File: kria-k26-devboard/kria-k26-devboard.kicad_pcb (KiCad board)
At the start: 8 copper layers, 118 x 100 mm, 476 parts, among them IC1 USB5534B-5000JZX, IC2 TPS2378DDA, J1 47272-0001, J10 USB4105-GF-A, J11 DC_SOCKET, J2 1140084168, J3 WE_68715014522, J4 SSW-106-02-G-D-RA, J5 5-2337992-8, J6 22-23-2021, J7 BM08B-SRSS-TB-LF-SN, J8 1050170001, J9 0878311420, M1 XILINX-KRIA-K26, P1 2199119-6, Q1 BSS123, Q10 BSS138-7-F, Q11 BSS138-7-F, Q12 DTC014TEBTL, Q13 DTC014TEBTL, Q14 DTC014TEBTL, Q15 PJA3441, Q16 BSS138-7-F, Q2 AO3401A, Q3 BSS138-7-F, Q4 BSS138DW-7-F, Q5 PJA3441, Q6 BSS138-7-F, Q7 BSS138-7-F, Q8 BSS138-7-F, Q9 BSS138-7-F, U1 SN74AVC4T245PWR, U10 PCA9306D_118, U11 M24C64-FMC6TG, U12 TPD4E05U06QDQARQ1, U13 TPD4E05U06QDQARQ1, U14 USB3310C-CP, U15 TPD4E05U06QDQARQ1, U16 TPD4E05U06QDQARQ1, U17 GSB3112311HR, U18 TPD4E05U06QDQARQ1, U19 TPD4E05U06QDQARQ1, U2 FIN1019MTC, U20 GSB3112311HR, U21 DP83867CRRGZR, U22 TPS3840PH30DBVR, U23 TPS3840PH30DBVR, U24 SN74AVC4T245PWR, U25 SN74AVC2T245RSWR, U26 SN74LVC1G125DBVR, U27 74LV07ATPWJ, U28 MCP1799-3302H_DB, U29 MCP1799-3302H_DB, U3 TPD4E05U06QDQARQ1, U30 FT4232HPQ, U31 93LC56CT-IMC, U32 SN74AVC4T245PWR, U33 SN74AVC4T245PWR, U34 SN74AVC2T245RSWR, U35 SN74AVC2T245RSWR, U36 NC7WZ07P6X, U37 RPX-4.0-R, U38 AP62301WU-7, U39 AP62301WU-7, U4 NVT4858HKZ, U40 AP62301WU-7, U41 AP62301WU-7, U42 AP62301WU-7, U43 AP62301WU-7, U44 AP62301WU-7, U45 AP62301WU-7, U46 LTC4358CDE, U47 LTC4358CDE, U48 LTC4358CDE, U5 TPS2116DRLR, U6 SI53152-A01AGMR, U7 SN65LVDS1DR, U8 XLL736027.000000X, U9 PI4MSD5V9540BUEX, Y1 SIT9120AI-2C3-33E100.000000X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

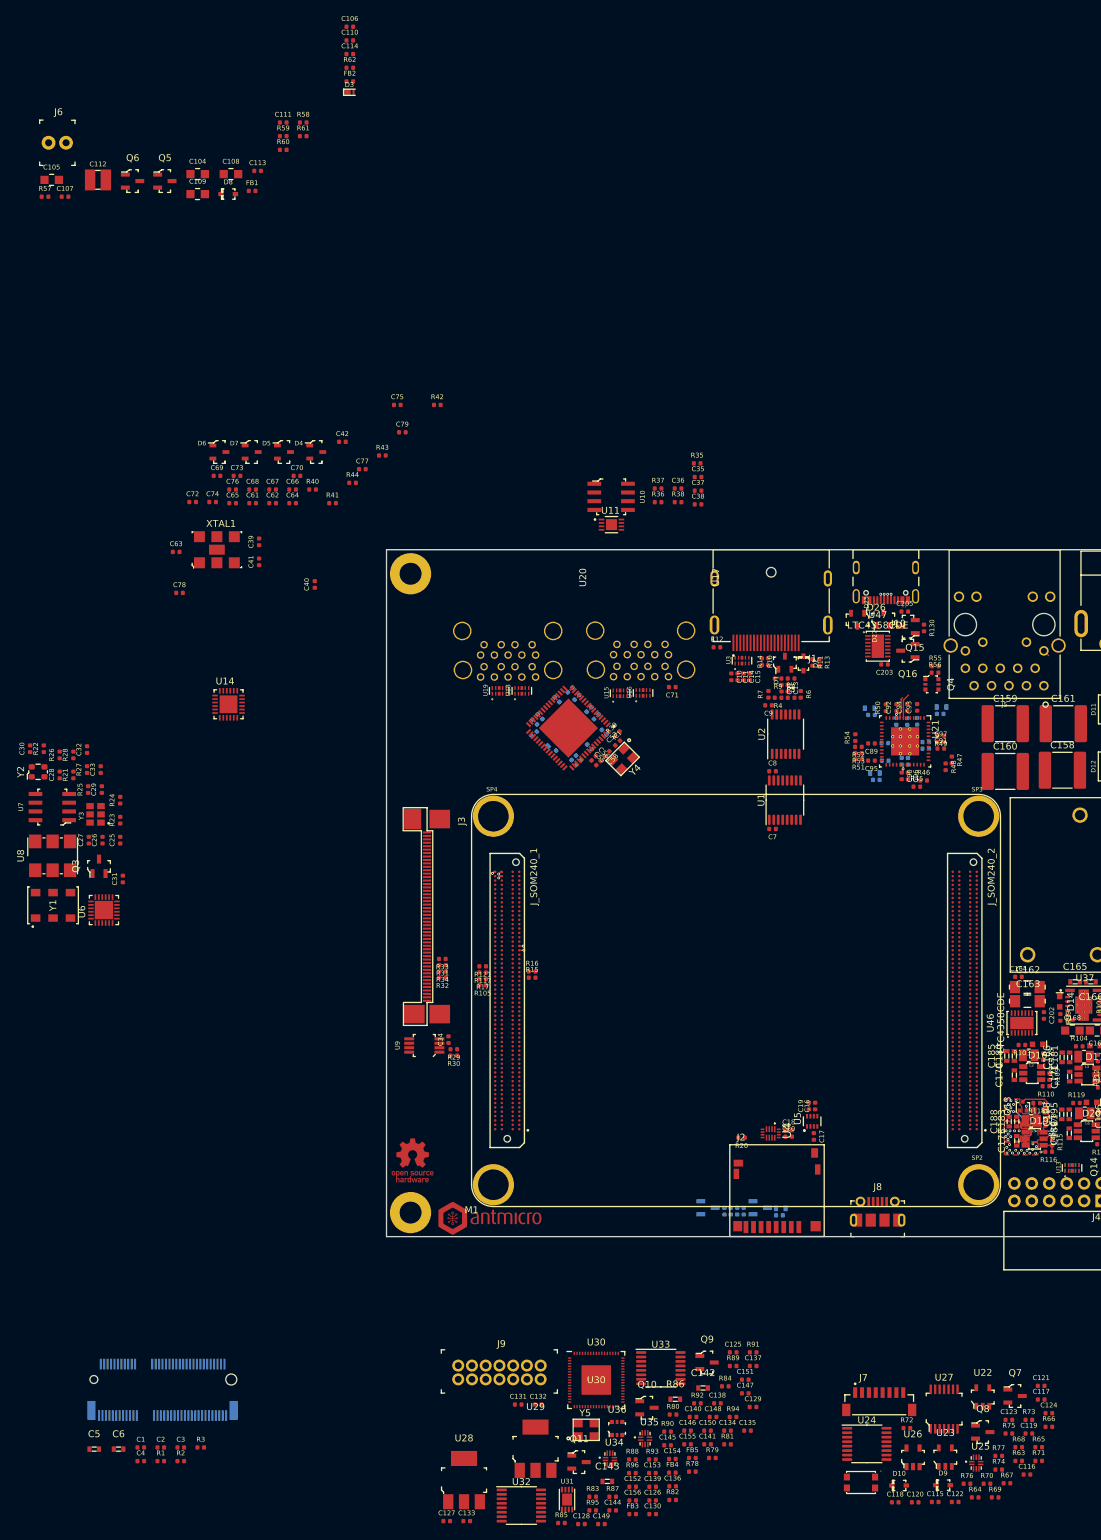
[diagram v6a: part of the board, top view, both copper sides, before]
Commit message: Finished initial component placement
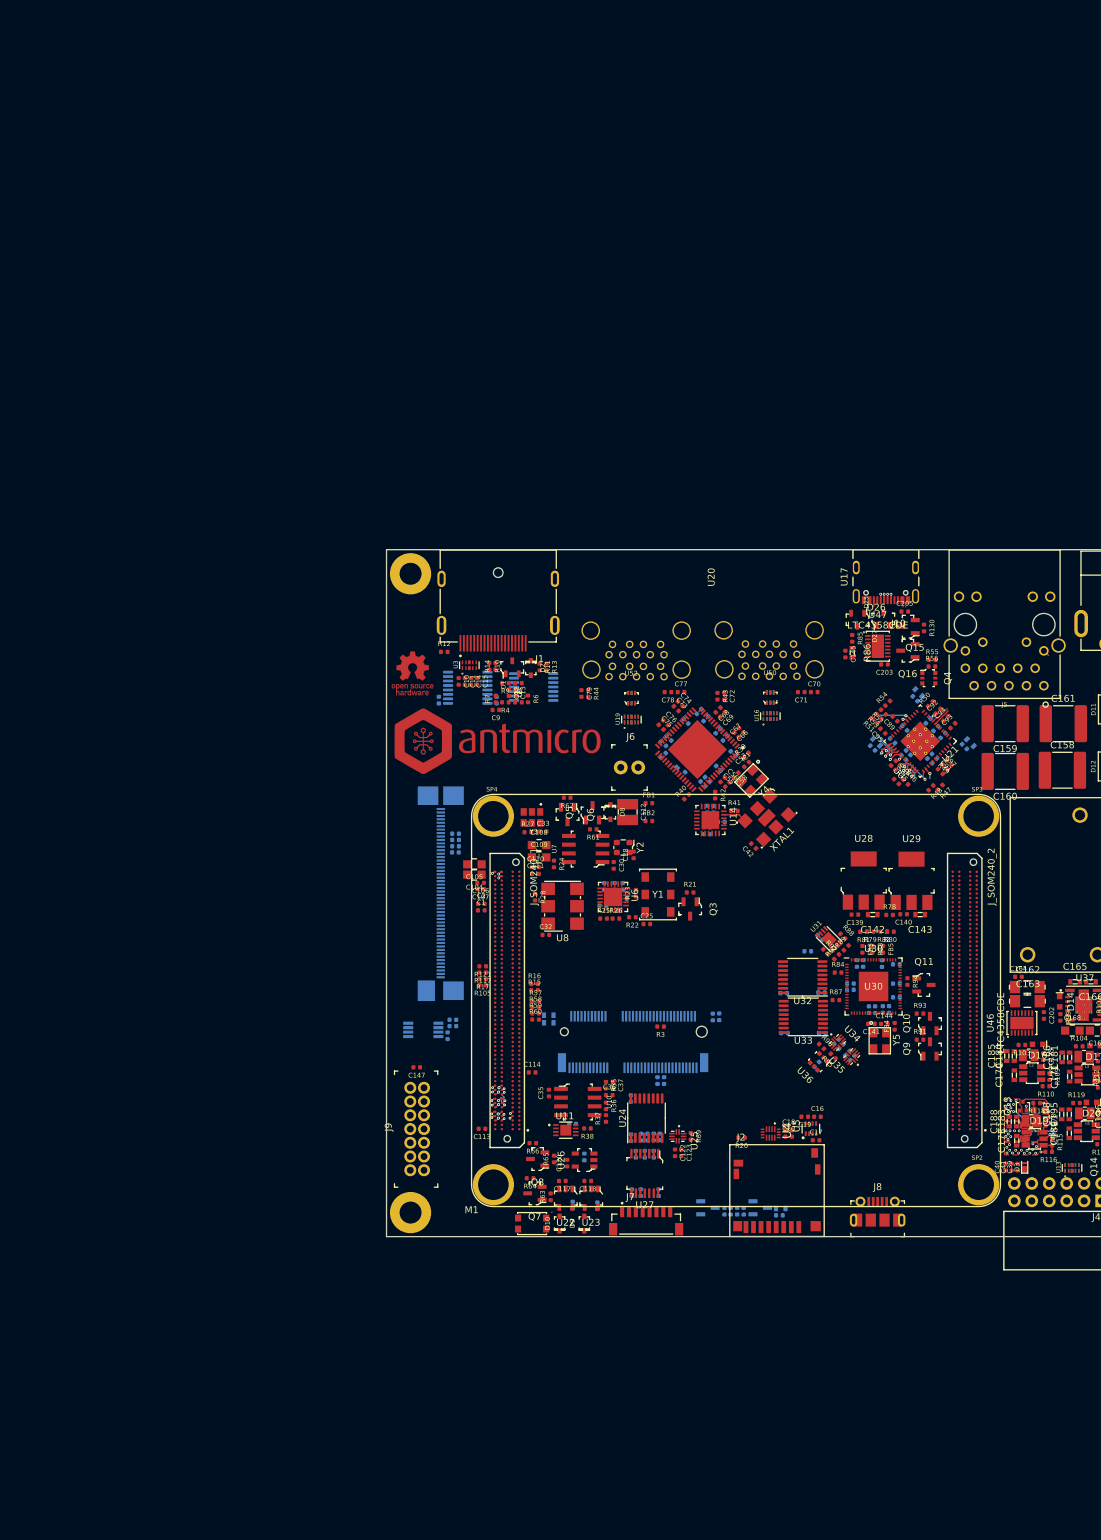
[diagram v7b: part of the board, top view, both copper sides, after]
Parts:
- removed D4, D5, D6, D7: PESD2USB5UV-TR, antmicro-footprints:SOT-23s
- added C207: C_100n_0402, antmicro-footprints:0402-cap, B.Cu at (107.7, 104.1)
- added U49: WE-TVS-82400152, antmicro-footprints:SOT-563, B.Cu at (129.9, 73.5)
- added U50: WE-TVS-82400152, antmicro-footprints:SOT-563, F.Cu at (129.9, 73.5)
- added U51: WE-TVS-82400152, antmicro-footprints:SOT-563, B.Cu at (109.7, 73.6)
- added U52: WE-TVS-82400152, antmicro-footprints:SOT-563, F.Cu at (109.7, 73.6)
- C115, C116, C119, C121, C124, C125, C126, C127, C128, C129, C130, C131, C132, C133, C134, C135, C136, C137, C138, C146, C148, C149, C150, C151, C152, C153, C154, C155, C156, C26, C27, C29, C3, C31, C34, C38, C4, C5, C6, C61, C62, C63, C64, C65, C7, C8, J3, R1, R2, R29, R30, R31, R32, R33, R34, R67, R68, R70, R71, R72, R73, R74, R75, R76, R77, U1, U15, U18, U2, U9: moved to B.Cu
- N2: footprint antmicro-footprints:antmicro-logo_scaled_15mm -> antmicro-footprints:antmicro-logo_scaled_30mm
- moved D3 184.8 mm to (166.9, 141.9), turned to 90 degrees
- moved C114 150.6 mm to (95.2, 128.1)
- moved C113 143.2 mm to (87.9, 136.3), turned to 180 degrees
- moved C39 143.1 mm to (165.9, 141.9)
- moved C41 140.6 mm to (165.0, 141.9)
- moved R57 137.2 mm to (95.7, 117.7)
- moved R85 135.6 mm to (141.8, 64.9), turned to 270 degrees
- moved R58 133.2 mm to (95.7, 118.6)
- moved R59 132.9 mm to (95.7, 119.5)
- moved R60 131.8 mm to (95.7, 120.4)
- moved C40 131.6 mm to (164.1, 141.9)
- moved C106 126.1 mm to (87.7, 100.5), turned to 180 degrees
- moved C110 123.3 mm to (95.7, 98.2)
- moved J6 123.3 mm to (108.1, 83.7)
- moved C112 120.1 mm to (109.1, 90.2), turned to 270 degrees
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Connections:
- C132 pad 1: GND -> PS_3V3
- C132 pad 2: /Debug and JTAG/USB_3V3 -> GND
- U17 pad 11: /USB/USB2_N -> Net-(U17-Pad11)
- U17 pad 12: /USB/USB2_P -> Net-(U17-Pad12)
- U17 pad 2: /USB/USB1_N -> Net-(U17-Pad2)
- U17 pad 3: /USB/USB1_P -> Net-(U17-Pad3)
- U20 pad 11: /USB/USB4_N -> Net-(U20-Pad11)
- U20 pad 12: /USB/USB4_P -> Net-(U20-Pad12)
- U20 pad 2: /USB/USB3_N -> Net-(U20-Pad2)
- U20 pad 3: /USB/USB3_P -> Net-(U20-Pad3)
- U27 pad 1: Net-(R68-Pad2) -> Net-(R69-Pad2)
- U27 pad 10: /PCIE M2 key E /~M2_PERST -> /Reset logic/~SD_CARD_RESET
- U27 pad 11: Net-(R69-Pad2) -> Net-(R68-Pad2)
- U27 pad 2: /Reset logic/~SD_CARD_RESET -> /PCIE M2 key E /~M2_PERST
- U27 pad 3: Net-(R70-Pad2) -> Net-(R72-Pad2)
- U27 pad 4: /Reset logic/~USB_PHY_RESET -> /Ethernet/~ETH_RESET
- U27 pad 8: /Ethernet/~ETH_RESET -> /Reset logic/~USB_PHY_RESET
- U27 pad 9: Net-(R72-Pad2) -> Net-(R70-Pad2)
- U30 pad 51: /Debug and JTAG/USB_3V3 -> Net-(U30-Pad51)
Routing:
- net /Ethernet/MIO69: track 0.00 -> 5.41 mm, vias 0 -> 1
- net /Ethernet/MIO65: track 0.00 -> 5.33 mm, vias 0 -> 1
- net /Camera interface/HPA04_P: track 0.00 -> 5.13 mm, vias 0 -> 1
- net /Ethernet/MIO66: track 0.00 -> 4.98 mm, vias 0 -> 1
- net /Ethernet/MIO76: track 0.00 -> 4.59 mm, vias 0 -> 1
- net /Camera interface/HPA04_N: track 0.00 -> 4.48 mm, vias 0 -> 1
- net /Camera interface/HPA02_P: track 0.00 -> 3.65 mm, vias 0 -> 1
- net /Camera interface/HPA02_N: track 0.00 -> 3.54 mm, vias 0 -> 1
- net GND: track 4.83 -> 8.36 mm, vias 16 -> 22
- net /Camera interface/HPA01_P: track 0.00 -> 3.51 mm, vias 0 -> 1
- net Net-(U14-Pad23): track 0.00 -> 3.46 mm
- net /Camera interface/HPA01_N: track 0.00 -> 3.33 mm, vias 0 -> 1
- net /Camera interface/HPA03_P: track 0.00 -> 2.53 mm, vias 0 -> 1
- net /Ethernet/MIO72: track 0.00 -> 2.30 mm, vias 0 -> 1
- net /Ethernet/MIO68: track 0.00 -> 2.23 mm, vias 0 -> 1
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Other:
- net class Default: via_dia 0.55 -> 0.45; via_drill 0.3 -> 0.2
- net class ipedance_internal added: clearance 0.125, trace_width 0.155, via_dia 0.4, via_drill 0.15

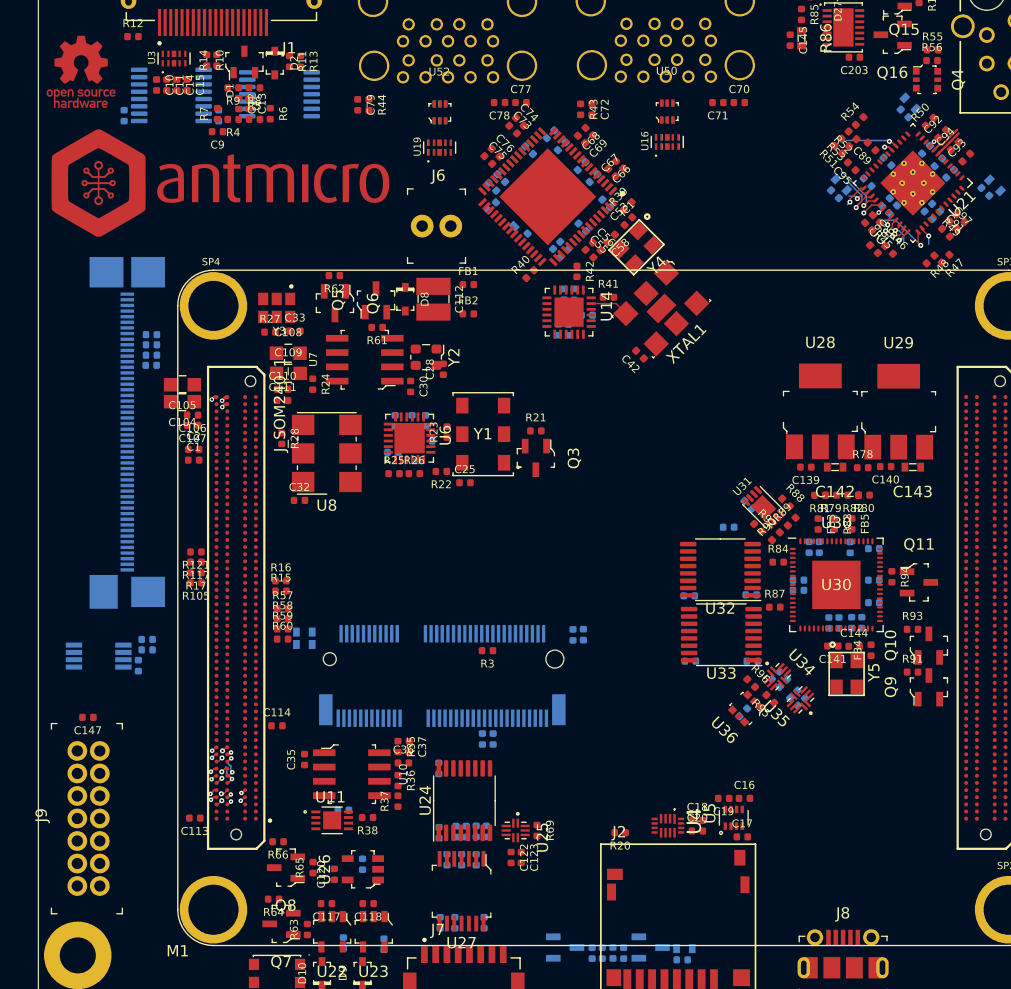
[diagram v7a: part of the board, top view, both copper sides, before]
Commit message: Component size optimization, SOM connector fanout, routing of camera interface
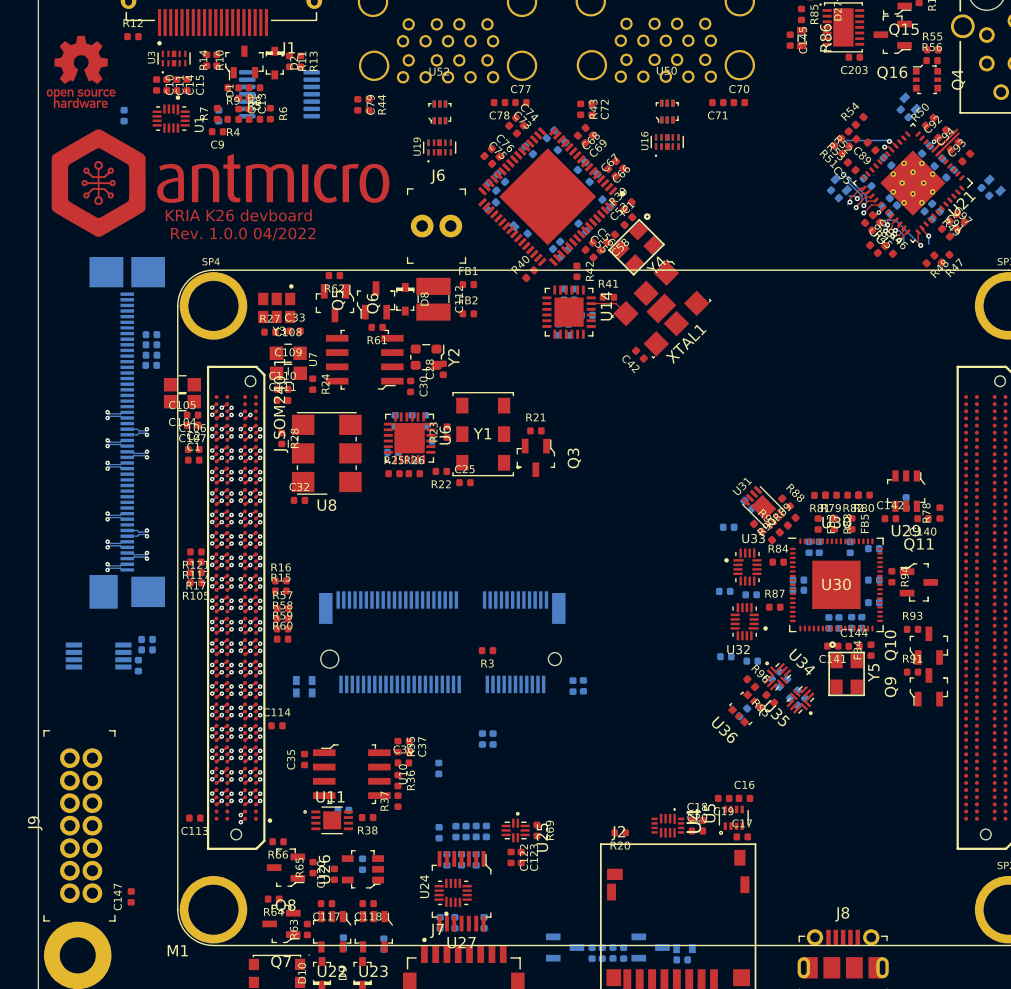
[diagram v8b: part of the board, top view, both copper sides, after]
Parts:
- removed C143: C_10u_0603, antmicro-footprints:0603-cap
- removed U28: MCP1799-3302H_DB, antmicro-footprints:SOT-223
- C139: moved to B.Cu
- C142: value C_10u_0603 -> C_100n_0402; footprint antmicro-footprints:0603-cap -> antmicro-footprints:0402-cap
- U1: value SN74AVC4T245PWR -> 74AVC4T245RSVRG4; footprint antmicro-footprints:TSSOP-16_4.4x5mm_P0.65mm -> antmicro-footprints:Texas_16-UFQFN; moved to F.Cu
- U24, U32, U33: value SN74AVC4T245PWR -> 74AVC4T245RSVRG4; footprint antmicro-footprints:TSSOP-16_4.4x5mm_P0.65mm -> antmicro-footprints:Texas_16-UFQFN
- U29: value MCP1799-3302H_DB -> MIC5211-3.3YM6-TR; footprint antmicro-footprints:SOT-223 -> antmicro-footprints:SOT-23-6
- moved C147 16.4 mm to (82.2, 143.3), turned to 90 degrees
- moved C139 9.46 mm to (151.1, 108.3), turned to 270 degrees
- moved U24 8.26 mm to (110.8, 142.9)
- moved R78 7.96 mm to (154.1, 109.2), turned to 90 degrees
- moved U29 7.09 mm to (151.1, 107.2), turned to 180 degrees
- moved C142 6.71 mm to (149.7, 109.7), turned to 0 degrees
- moved U33 6.44 mm to (137.0, 114.0), turned to 0 degrees
- moved C140 5.70 mm to (152.6, 109.7)
- moved U32 5.09 mm to (136.8, 118.8)
- moved C3 4.55 mm to (122.4, 124.5)
- moved C4 4.55 mm to (121.5, 124.6)
- moved C5 4.30 mm to (97.6, 125.2)
- moved C6 4.30 mm to (97.6, 124.1)
- moved C155 3.18 mm to (135.1, 122.0)
- moved C154 3.18 mm to (135.0, 116.2)
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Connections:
- C140 pad 2: /Debug and JTAG/USBB_VBUS -> /Debug and JTAG/PD_3V3
- C142 pad 1: /Debug and JTAG/PD_3V3 -> GND
- C142 pad 2: GND -> /Debug and JTAG/USB_3V3
- U1 pad 1: PS_1V8 -> GND
- U1 pad 10: /Display Port/DP_HPD -> GND
- U1 pad 11: /Display Port/DP_AUX_IN -> GND
- U1 pad 12: /Display Port/DP_OE -> /Display Port/DP_HPD
- U1 pad 13: /Display Port/DP_AUX_OUT -> /Display Port/DP_AUX_IN
- U1 pad 14: GND -> /Display Port/DP_OE
- U1 pad 15: GND -> /Display Port/DP_AUX_OUT
- U1 pad 16: PS_3V3 -> GND
- U1 pad 2: PS_1V8 -> PS_3V3
- U1 pad 3: GND -> PS_1V8
- U1 pad 4: /Display Port/MIO27 -> PS_1V8
- U1 pad 5: /Display Port/MIO29 -> GND
- U1 pad 6: /Display Port/MIO30 -> /Display Port/MIO27
- U1 pad 7: /Display Port/MIO28 -> /Display Port/MIO29
- U1 pad 8: GND -> /Display Port/MIO30
- U1 pad 9: GND -> /Display Port/MIO28
- U24 pad 1: PS_3V3 -> /Reset logic/PS_RST
- U24 pad 10: /Reset logic/MIO38 -> GND
- U24 pad 11: /Reset logic/MIO44 -> GND
- U24 pad 12: /Reset logic/MIO44 -> /Reset logic/MIO38
- U24 pad 13: /Reset logic/MIO43 -> /Reset logic/MIO44
- U24 pad 14: /Reset logic/PS_RST -> /Reset logic/MIO44
- U24 pad 15: /Reset logic/PS_RST -> /Reset logic/MIO43
- U24 pad 16: PS_1V8 -> /Reset logic/PS_RST
- U24 pad 2: GND -> PS_1V8
- U24 pad 3: GND -> PS_3V3
- U24 pad 4: Net-(R68-Pad2) -> GND
- U24 pad 5: Net-(R70-Pad2) -> GND
- U24 pad 6: Net-(R71-Pad2) -> Net-(R68-Pad2)
- U24 pad 7: Net-(R72-Pad2) -> Net-(R70-Pad2)
- U24 pad 8: GND -> Net-(R71-Pad2)
- U24 pad 9: GND -> Net-(R72-Pad2)
- U29 pad 1: /Debug and JTAG/USBB_VBUS -> VBUS
- U29 pad 3: /Debug and JTAG/USB_3V3 -> VBUS
- U29 pad 4: GND -> /Debug and JTAG/USB_3V3
- U30 pad 51: Net-(U30-Pad51) -> /Debug and JTAG/USB_3V3
- U32 pad 1: /Debug and JTAG/USB_3V3 -> /Debug and JTAG/~LS_OE
- U32 pad 10: Net-(U32-Pad10) -> GND
- U32 pad 11: /Debug and JTAG/JTAG_TDI_C2M -> GND
- U32 pad 12: /Debug and JTAG/JTAG_TCK_C2M -> Net-(U32-Pad12)
- U32 pad 13: /Debug and JTAG/JTAG_TMS_C2M -> /Debug and JTAG/JTAG_TDI_C2M
- U32 pad 14: /Debug and JTAG/~LS_OE -> /Debug and JTAG/JTAG_TCK_C2M
- U32 pad 15: /Debug and JTAG/~LS_OE -> /Debug and JTAG/JTAG_TMS_C2M
- U32 pad 16: PS_1V8 -> /Debug and JTAG/~LS_OE
- U32 pad 2: /Debug and JTAG/USB_PWRD_VCCIO -> PS_1V8
- U32 pad 3: /Debug and JTAG/USB_PWRD_VCCIO -> /Debug and JTAG/USB_3V3
- U32 pad 4: /Debug and JTAG/FTDI_TMS -> /Debug and JTAG/USB_PWRD_VCCIO
- U32 pad 5: /Debug and JTAG/FTDI_TCK -> /Debug and JTAG/USB_PWRD_VCCIO
- U32 pad 6: /Debug and JTAG/FTDI_TDI -> /Debug and JTAG/FTDI_TMS
- U32 pad 7: GND -> /Debug and JTAG/FTDI_TCK
- U32 pad 8: GND -> /Debug and JTAG/FTDI_TDI
- U33 pad 1: /Debug and JTAG/USB_3V3 -> /Debug and JTAG/~LS_OE
- U33 pad 11: PS_1V8 -> GND
- U33 pad 13: /Debug and JTAG/JTAG_TDO_M2C -> PS_1V8
- U33 pad 15: /Debug and JTAG/~LS_OE -> /Debug and JTAG/JTAG_TDO_M2C
- U33 pad 16: PS_1V8 -> GND
- U33 pad 2: GND -> PS_1V8
- U33 pad 3: GND -> /Debug and JTAG/USB_3V3
- U33 pad 4: /Debug and JTAG/FTDI_TDO -> GND
- U33 pad 5: Net-(U33-Pad5) -> GND
- U33 pad 6: /Debug and JTAG/JTAG_VCCO_ON -> /Debug and JTAG/FTDI_TDO
- U33 pad 8: GND -> /Debug and JTAG/JTAG_VCCO_ON
- U33 pad 9: GND -> Net-(U33-Pad9)
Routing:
- net /Camera interface/HPA06_P: track 0.00 -> 55.2 mm, vias 0 -> 2
- net /Camera interface/HPA06_N: track 0.00 -> 54.8 mm, vias 0 -> 2
- net /Camera interface/HPA05_CC_P: track 0.00 -> 52.2 mm, vias 0 -> 2
- net /Camera interface/HPA05_CC_N: track 0.00 -> 51.7 mm, vias 0 -> 2
- net /Camera interface/HPA07_P: track 0.00 -> 45.2 mm, vias 0 -> 2
- net /Camera interface/HPA07_N: track 0.00 -> 44.9 mm, vias 0 -> 2
- net /Camera interface/HPA08_P: track 0.47 -> 43.8 mm, vias 1 -> 2
- net /Camera interface/HPA08_N: track 0.40 -> 43.5 mm, vias 1 -> 2
- net /Camera interface/HPA00_CC_P: track 0.50 -> 40.7 mm, vias 1 -> 2
- net /Camera interface/HPA00_CC_N: track 0.52 -> 40.4 mm, vias 1 -> 2
- net GND: track 8.36 -> 43.6 mm, vias 22 -> 87
- net /Camera interface/HPA01_P: track 3.51 -> 38.3 mm, vias 1 -> 2
- net /Camera interface/HPA01_N: track 3.33 -> 37.5 mm, vias 1 -> 2
- net /Camera interface/HPA09_P: track 0.53 -> 34.6 mm, vias 1 -> 2
- net /Camera interface/HPA03_P: track 2.53 -> 36.5 mm, vias 1 -> 2
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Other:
- net class Default: clearance 0.125 -> 0.1; trace_width 0.125 -> 0.2; via_dia 0.45 -> 0.4; via_drill 0.2 -> 0.15
- net class ipedance_internal: clearance 0.125 -> 0.1; trace_width 0.155 -> 0.1
- rule trace_clearance: 0.125 -> 0.1
- rule trace_min: 0.125 -> 0.1
- board text added: "KRIA K26 devboard"
- board text added: "Rev. 1.0.0 04/2022"
